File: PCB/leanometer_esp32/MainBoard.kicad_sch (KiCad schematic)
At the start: 39 parts, among them J1 DM3AT-SF-PEJM5, J2 MPU6050, J3 PROG, J4 VBAT, J5 Conn_01x07, SW1 SW_Push, SW2 SW_Push, SW3 SW_Push, U1 ESP32-WROOM-32D, U2 LD1117S33TR_SOT223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

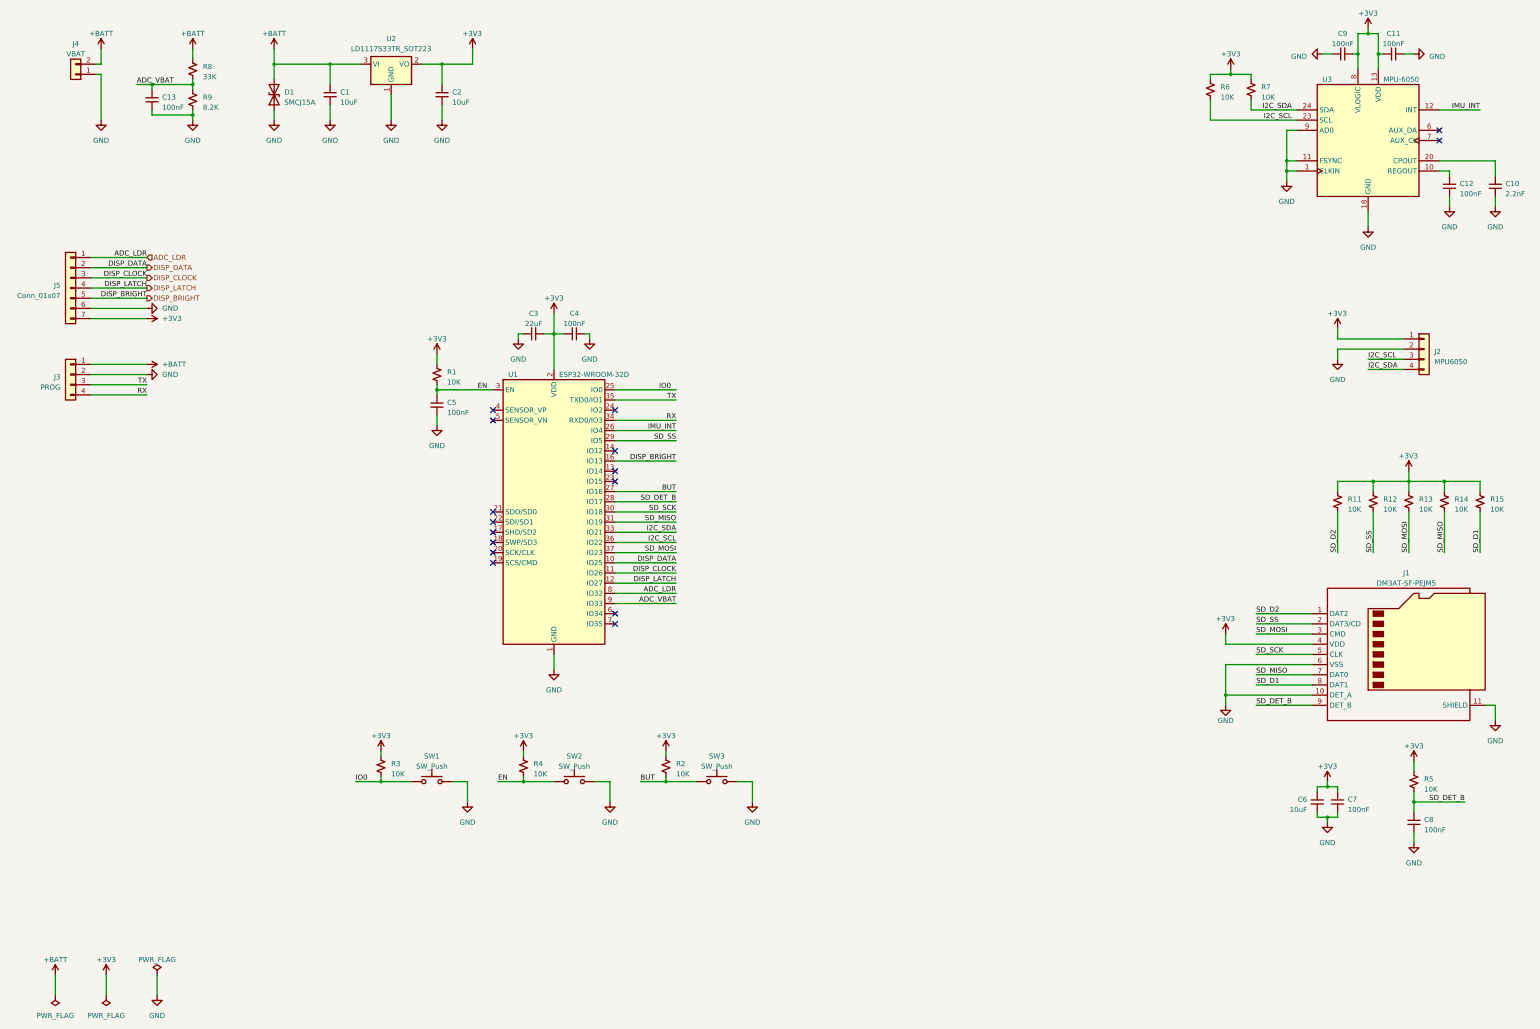
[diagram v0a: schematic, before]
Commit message: Added PowerBoard hierarchical sheet, completed layout
Signed-off-by: theloukou
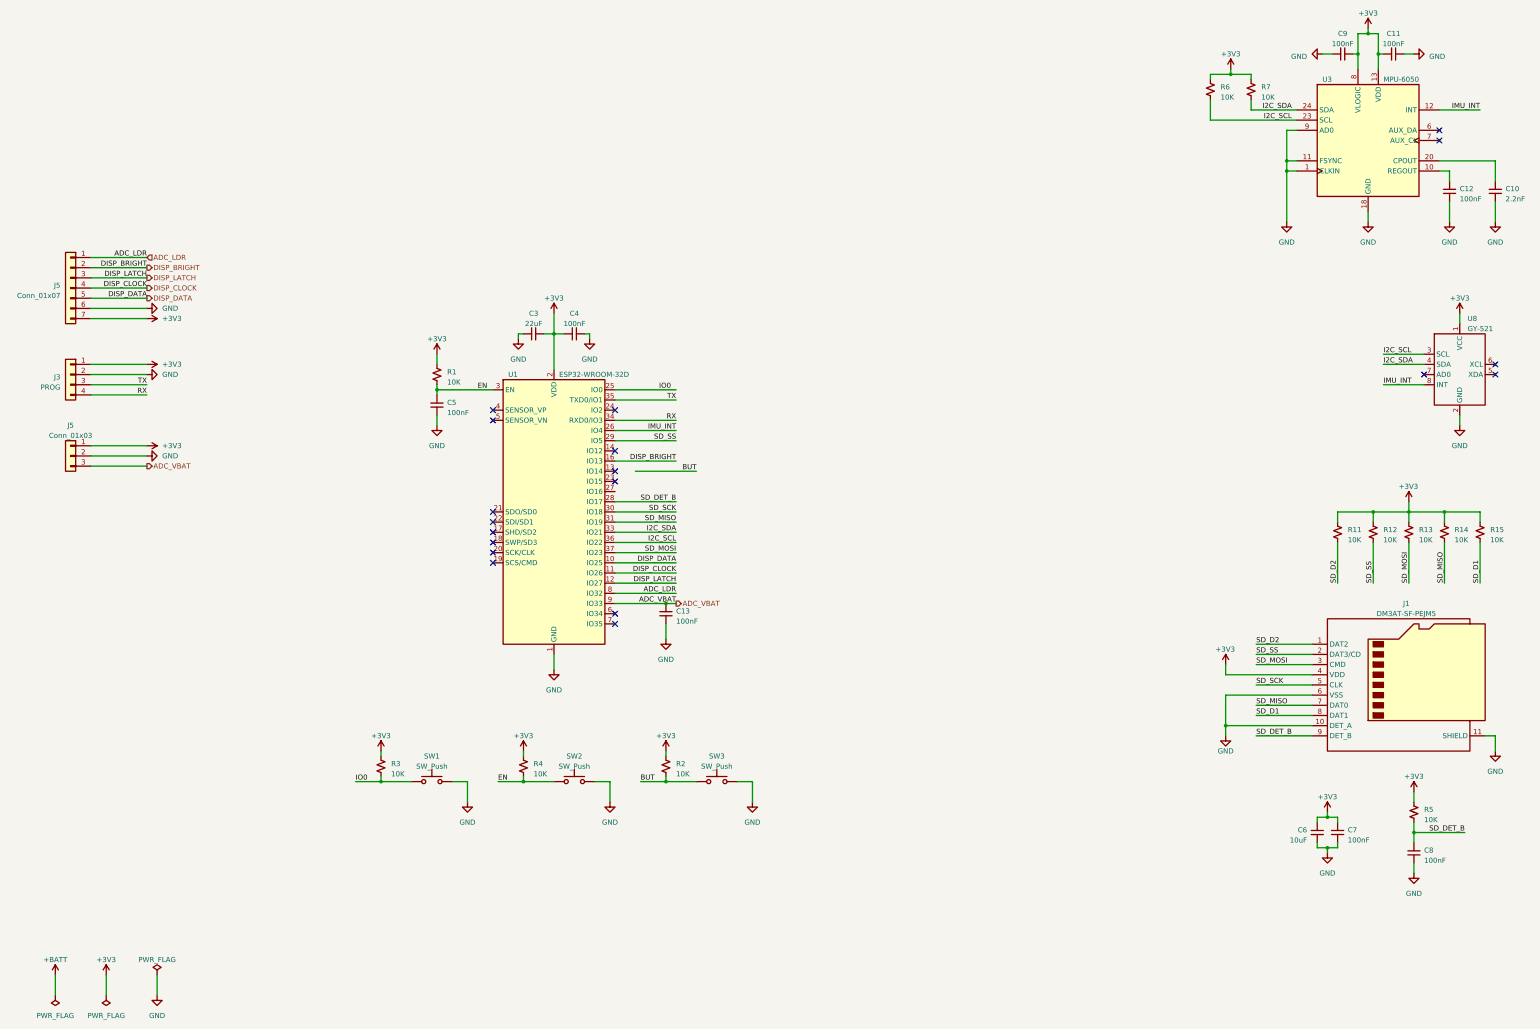
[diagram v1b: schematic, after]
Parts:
- removed C1, C2: 10uF, Capacitor_SMD:C_0805_2012Metric, symbol Device:C_Small
- removed D1: SMCJ15A, Diode_SMD:D_SMC, symbol Device:D_TVS
- removed J2: MPU6050, Connector_PinHeader_2.54mm:PinHeader_1x04_P2.54mm_Vertical, symbol Connector_Generic:Conn_01x04
- removed J4: VBAT, Connector_JST:JST_PH_S2B-PH-K_1x02_P2.00mm_Horizontal, symbol Connector_Generic:Conn_01x02
- removed R8: 33K, Resistor_SMD:R_0603_1608Metric, symbol Device:R_Small_US
- removed R9: 8.2K, Resistor_SMD:R_0603_1608Metric, symbol Device:R_Small_US
- removed U2: LD1117S33TR_SOT223, Package_TO_SOT_SMD:SOT-223-3_TabPin2, symbol Regulator_Linear:LD1117S33TR_SOT223
- added J5: Conn_01x03, Connector_PinHeader_2.54mm:PinHeader_1x03_P2.54mm_Vertical, symbol Connector_Generic:Conn_01x03
- added U8: GY-521, MPU6050(GY-521):GY-521_NoSlave+AD0, symbol MPU6050(GY-521):MPU6050(GY-521)
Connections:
- net +3V3: now also J3.1 (Pin_1), J5.1 (Pin_1), U8.1 (VCC)
- net +BATT: no longer J3.1 (Pin_1)
- net ADC_VBAT: now also J5.3 (Pin_3)
- net BUT: no longer U1.27 (IO16)
- net DISP_BRIGHT: now also J5.2 (Pin_2); no longer J5.5 (Pin_5)
- net DISP_CLOCK: now also J5.4 (Pin_4); no longer J5.3 (Pin_3)
- net DISP_DATA: now also J5.5 (Pin_5); no longer J5.2 (Pin_2)
- net DISP_LATCH: now also J5.3 (Pin_3); no longer J5.4 (Pin_4)
- net GND: now also J5.2 (Pin_2), U8.2 (GND)
- net I2C_SCL: now also U8.3 (SCL)
- net I2C_SDA: now also U8.4 (SDA)
- net IMU_INT: now also U8.8 (INT)
- no-connect marks 16 -> 19
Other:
- moved on the sheet: C10, C12, C6, C7, C8, J1, R11, R12, R13, R14, R15, R5

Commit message: Full layout rework
Signed-off-by: theloukou
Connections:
- net BUT: now also U1.27 (IO16)
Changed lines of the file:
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@@
     (stroke (width 0) (type default))
   )
-  (wire (pts (xy 176.53 138.43) (xy 191.77 138.43))
+  (wire (pts (xy 171.45 143.51) (xy 186.69 143.51))
     (stroke (width 0) (type default))
   )
@@
     (effects (font (size 1.27 1.27)) (justify right bottom))
   )
-  (label "BUT" (at 191.77 138.43 180) (fields_autoplaced)
-    (effects (font (size 1.27 1.27)) (justify right bottom))
-  )
+  (label "BUT" (at 186.69 143.51 180) (fields_autoplaced)
+    (effects (font (size 1.27 1.27)) (justify right bottom))
+  )

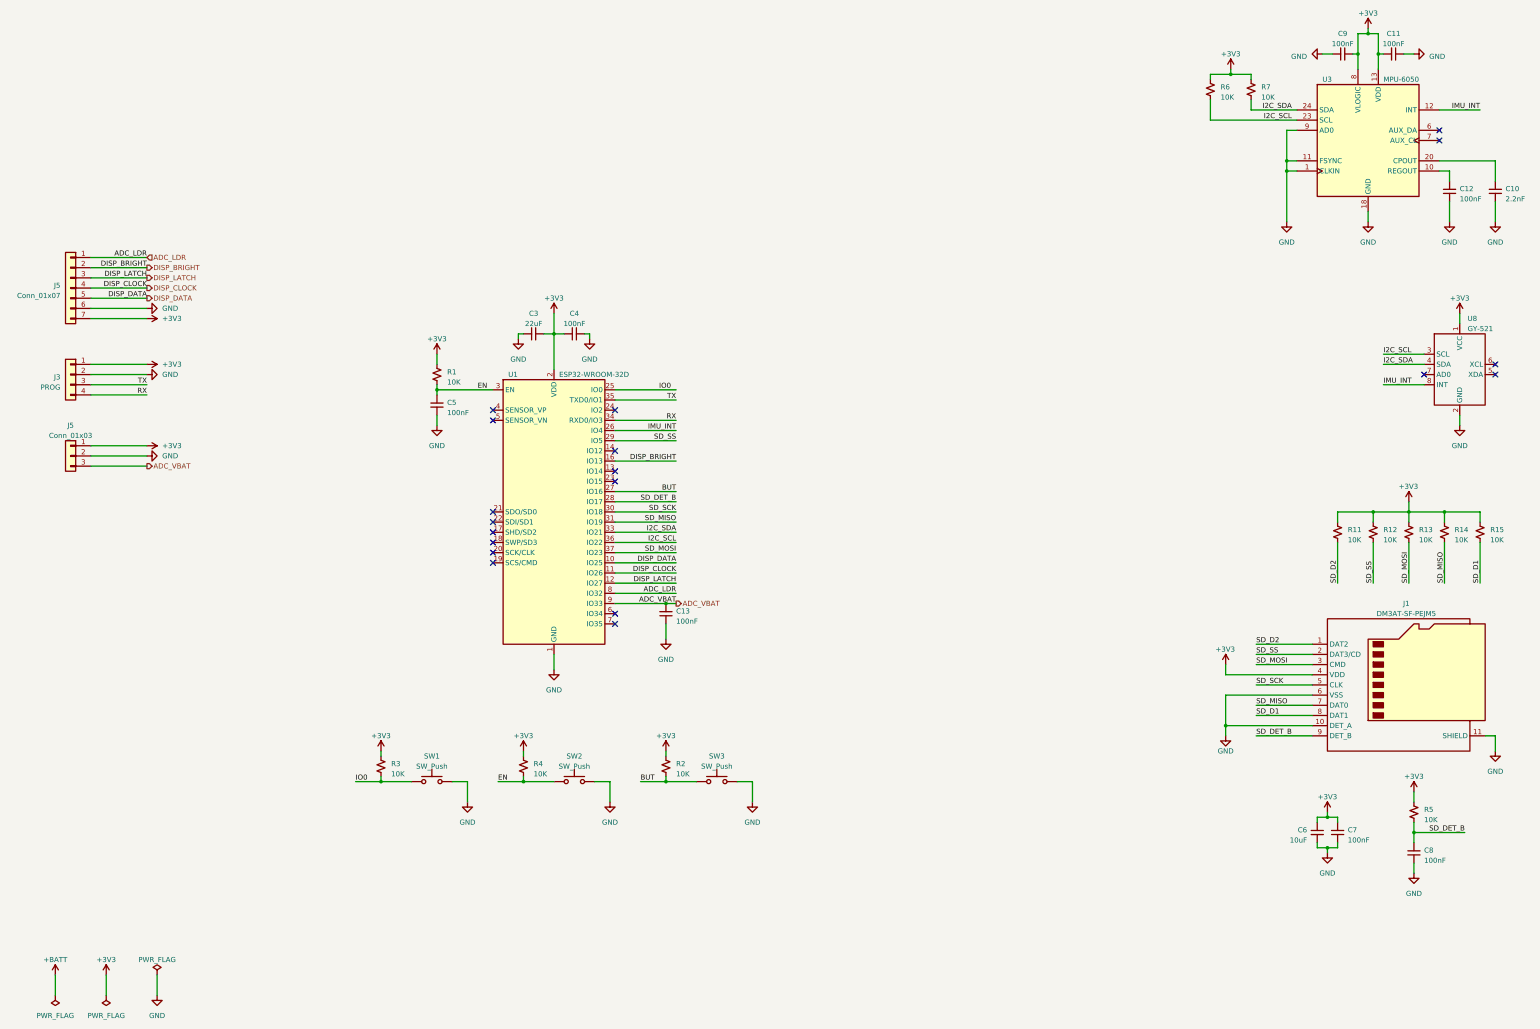
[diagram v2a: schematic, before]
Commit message: Added decoupling cap on ADC_LDR signal
Signed-off-by: theloukou
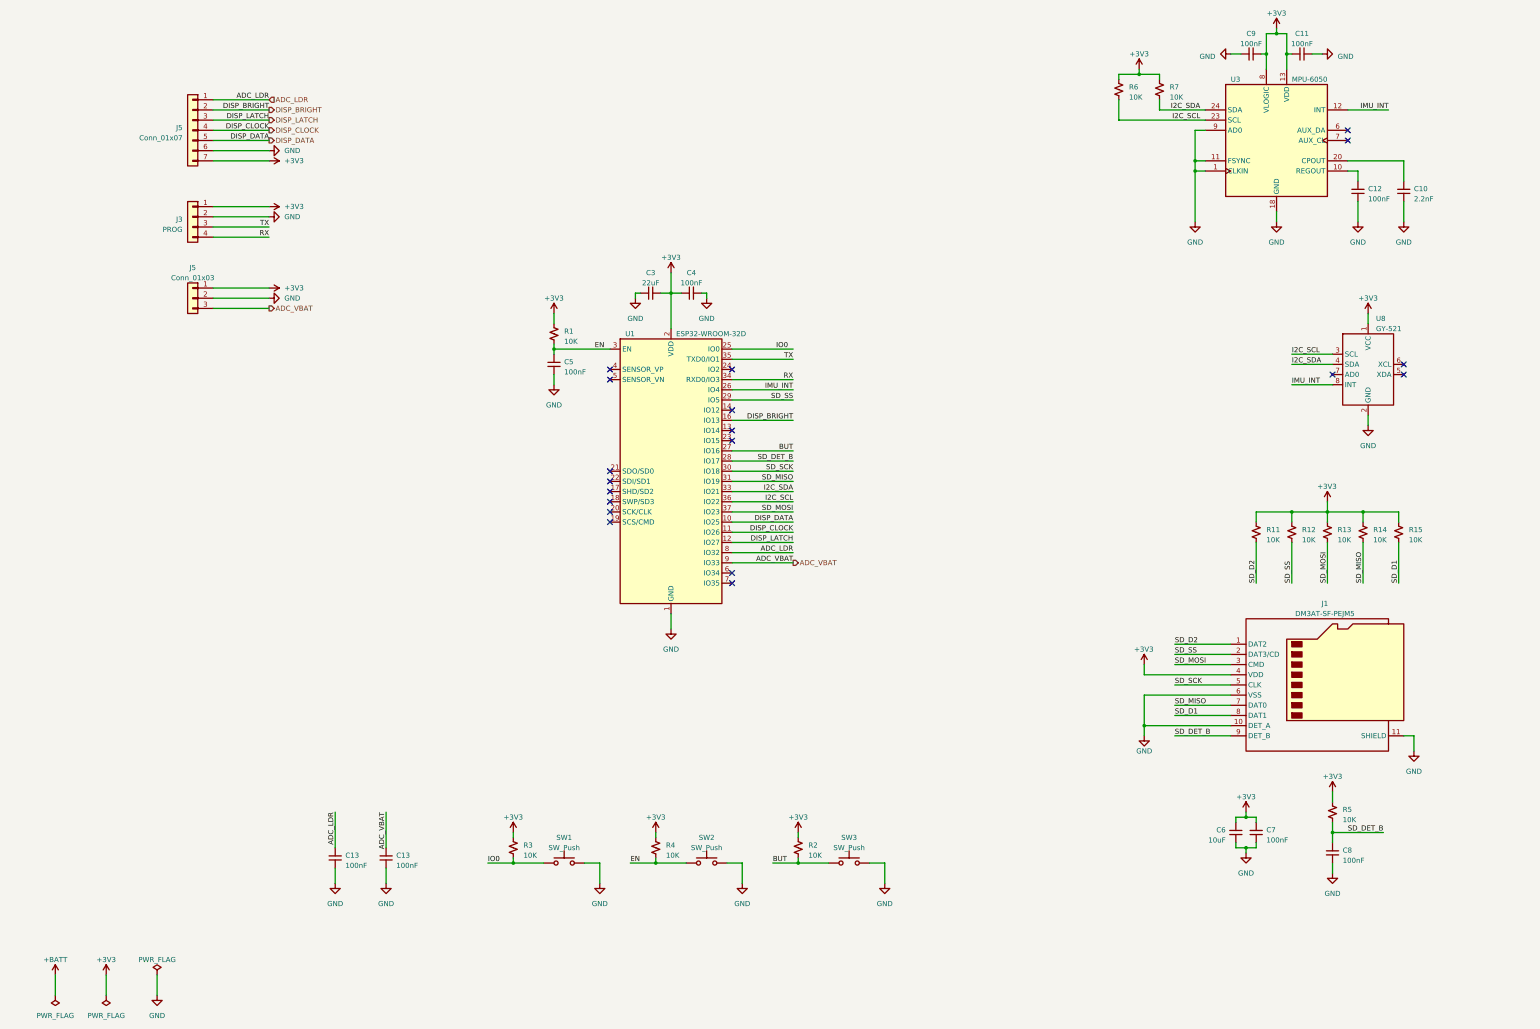
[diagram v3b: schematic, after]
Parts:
- added C13: 100nF, Capacitor_SMD:C_0603_1608Metric, symbol Device:C_Small
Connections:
- net ADC_LDR: now also C13.2
- net GND: now also C13.1
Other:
- moved on the sheet: C10, C11, C12, C13, C3, C4, C5, C6, C7, C8, C9, J1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
